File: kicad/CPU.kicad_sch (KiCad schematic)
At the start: 7 parts

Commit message: KiCad updates
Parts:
- removed U? (x6): 74LS245, symbol 74xx:74LS245
- added U? (x2): AS6C4008-55PCN, Package_DIP:DIP-32_W15.24mm, symbol Memory_RAM:AS6C4008-55PCN
- added U? (x2): SST39SF040, symbol Memory_Flash:SST39SF040
- added U?: GAL22V10, symbol Lattice_GAL_sym:GAL22V10
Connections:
- net A1: now also U?.12 (A0), U?.12 (A0), U?.12 (A0), U?.12 (A0)
- net A10: now also U?.26 (A9), U?.26 (A9), U?.26 (A9), U?.26 (A9)
- net A11: now also U?.23 (A10), U?.23 (A10), U?.23 (A10), U?.23 (A10)
- net A12: now also U?.25 (A11), U?.25 (A11), U?.25 (A11), U?.25 (A11)
- net A13: now also U?.4 (A12), U?.4 (A12), U?.4 (A12), U?.4 (A12)
- net A14: now also U?.28 (A13), U?.28 (A13), U?.28 (A13), U?.28 (A13)
- net A15: now also U?.29 (A14), U?.29 (A14), U?.3 (A14), U?.3 (A14)
- net A16: now also U?.3 (A15), U?.3 (A15), U?.31 (A15), U?.31 (A15)
- net A17: now also U?.2 (A16), U?.2 (A16), U?.2 (A16), U?.2 (A16)
- net A18: now also U?.30 (A17), U?.30 (A17), U?.30 (A17), U?.30 (A17)
- net A19: now also U?.1 (A18), U?.1 (A18), U?.1 (A18), U?.1 (A18)
- net A2: now also U?.11 (A1), U?.11 (A1), U?.11 (A1), U?.11 (A1)
- net A20: now also U?.2 (I1)
- net A21: now also U?.3 (I2)
- net A22: now also U?.4 (I3)
- net A23: now also U?.5 (I4)
- net A3: now also U?.10 (A2), U?.10 (A2), U?.10 (A2), U?.10 (A2)
- net A4: now also U?.9 (A3), U?.9 (A3), U?.9 (A3), U?.9 (A3)
- net A5: now also U?.8 (A4), U?.8 (A4), U?.8 (A4), U?.8 (A4)
- net A6: now also U?.7 (A5), U?.7 (A5), U?.7 (A5), U?.7 (A5)
- net A7: now also U?.6 (A6), U?.6 (A6), U?.6 (A6), U?.6 (A6)
- net A8: now also U?.5 (A7), U?.5 (A7), U?.5 (A7), U?.5 (A7)
- net A9: now also U?.27 (A8), U?.27 (A8), U?.27 (A8), U?.27 (A8)
- net D0: now also U?.13 (D0), U?.13 (DQ0)
- net D1: now also U?.14 (D1), U?.14 (DQ1)
- net D10: now also U?.15 (D2), U?.15 (DQ2)
- net D11: now also U?.17 (D3), U?.17 (DQ3)
- net D12: now also U?.18 (D4), U?.18 (DQ4)
- net D13: now also U?.19 (D5), U?.19 (DQ5)
- net D14: now also U?.20 (D6), U?.20 (DQ6)
- net D15: now also U?.21 (D7), U?.21 (DQ7)
- net D2: now also U?.15 (D2), U?.15 (DQ2)
- net D3: now also U?.17 (D3), U?.17 (DQ3)
- net D4: now also U?.18 (D4), U?.18 (DQ4)
- net D5: now also U?.19 (D5), U?.19 (DQ5)
- net D6: now also U?.20 (D6), U?.20 (DQ6)
- net D7: now also U?.21 (D7), U?.21 (DQ7)
- net D8: now also U?.13 (D0), U?.13 (DQ0)
- net D9: now also U?.14 (D1), U?.14 (DQ1)
- net GND: now also U?.12 (GND), U?.16 (GND), U?.16 (GND), U?.16 (VSS), U?.16 (VSS)
- net R/~{W}: now also U?.9 (R/W), U?.8 (I7)
- net VCC: now also U?.24 (VCC), U?.31 (PGM), U?.31 (PGM), U?.32 (VCC), U?.32 (VCC), U?.32 (VCC), U?.32 (VCC)
- net ~{AS}: now also U?.6 (AS), U?.6 (I5)
- net ~{LDS}: now also U?.8 (LDS), U?.7 (I6)
- net ~{UDS}: now also U?.7 (UDS), U?.9 (I8)
- new net ~{DUARTSEL}: U?.16 (I/O)
- new net ~{EVENREAD}: U?.18 (I/O), U?.24 (OE#), U?.24 (OE)
- new net ~{EVENWRITE}: U?.19 (I/O), U?.29 (WE#)
- new net ~{ODDREAD}: U?.17 (I/O), U?.24 (OE#), U?.24 (OE)
- new net ~{ODDWRITE}: U?.21 (I/O), U?.29 (WE#)
- new net ~{RAM0SEL}: U?.15 (I/O), U?.22 (CE#), U?.22 (CE#)
- new net ~{ROMSEL}: U?.14 (I/O), U?.22 (CE)
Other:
- note added: "EVEN"
- note added: "ODD"

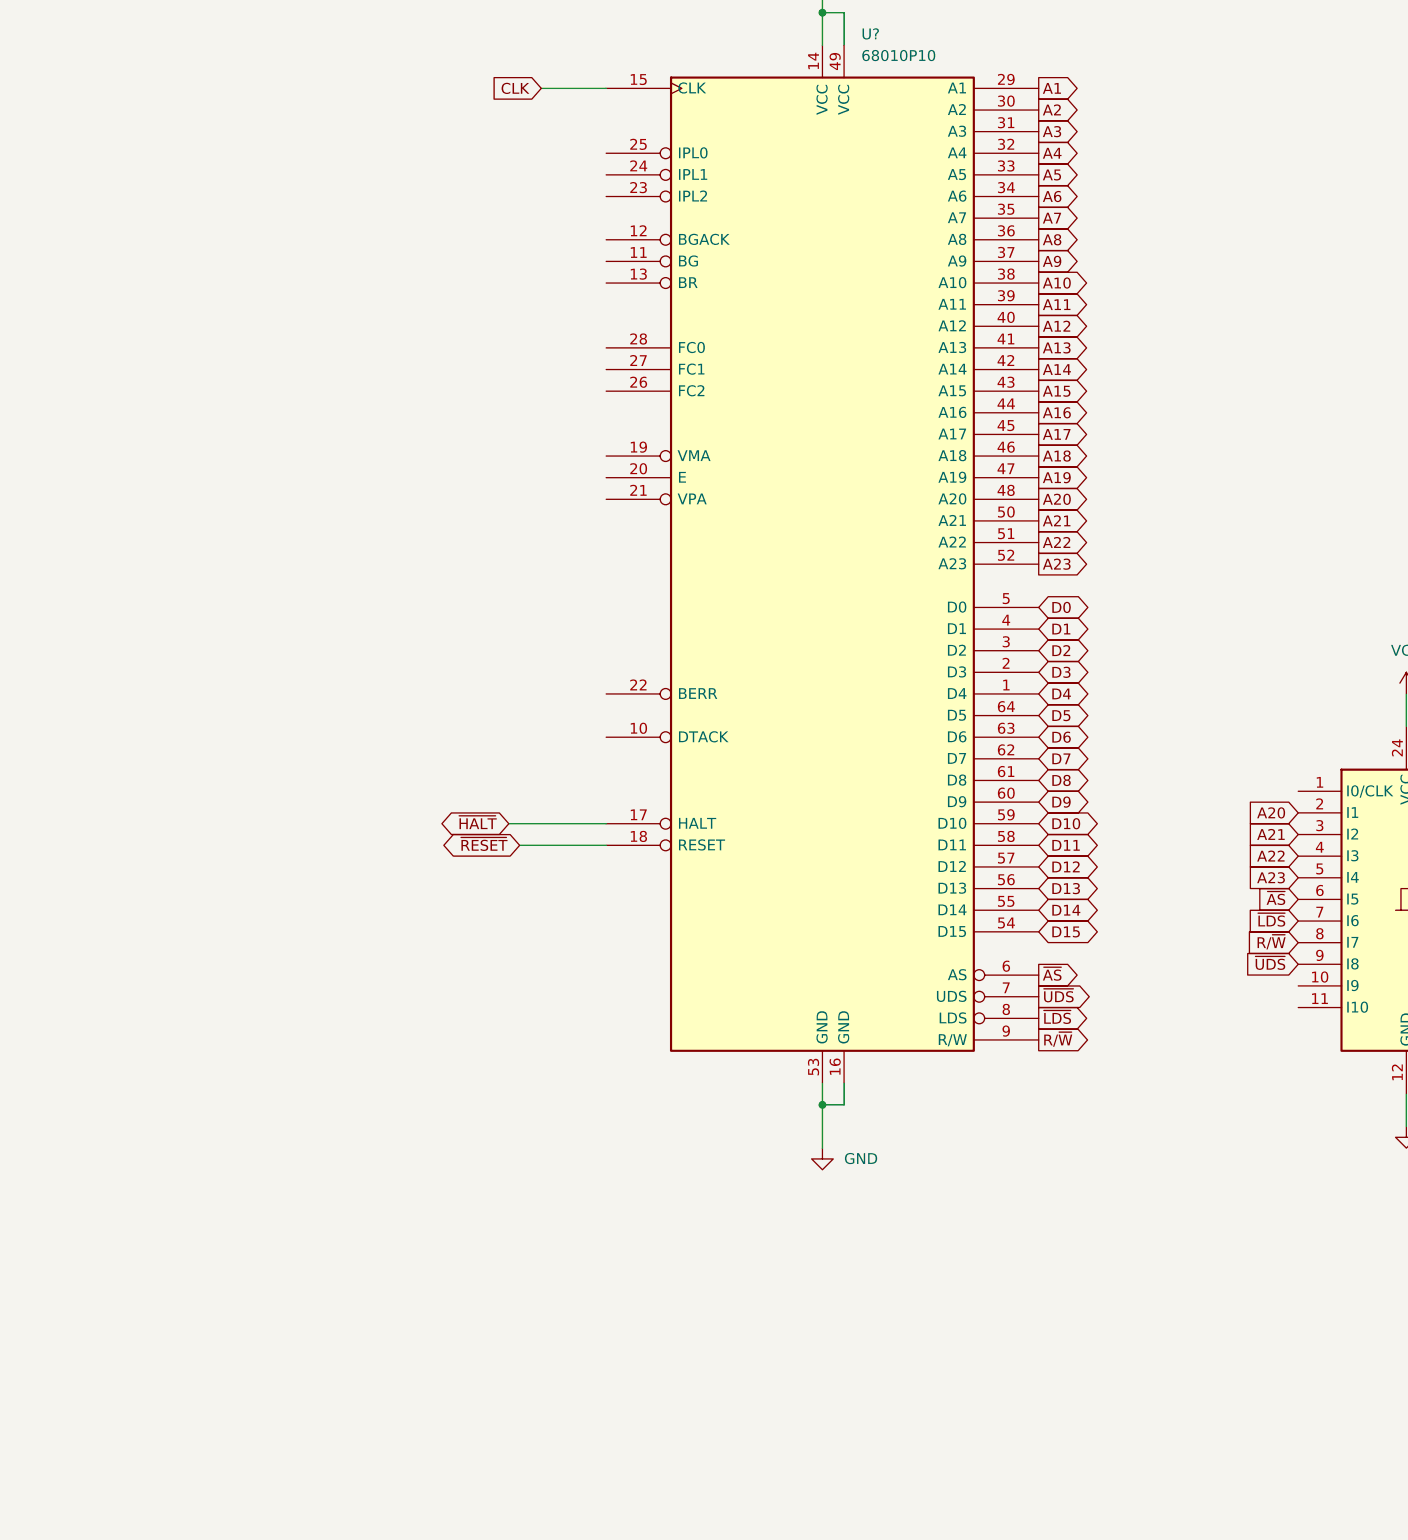
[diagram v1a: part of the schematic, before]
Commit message: Update kicad
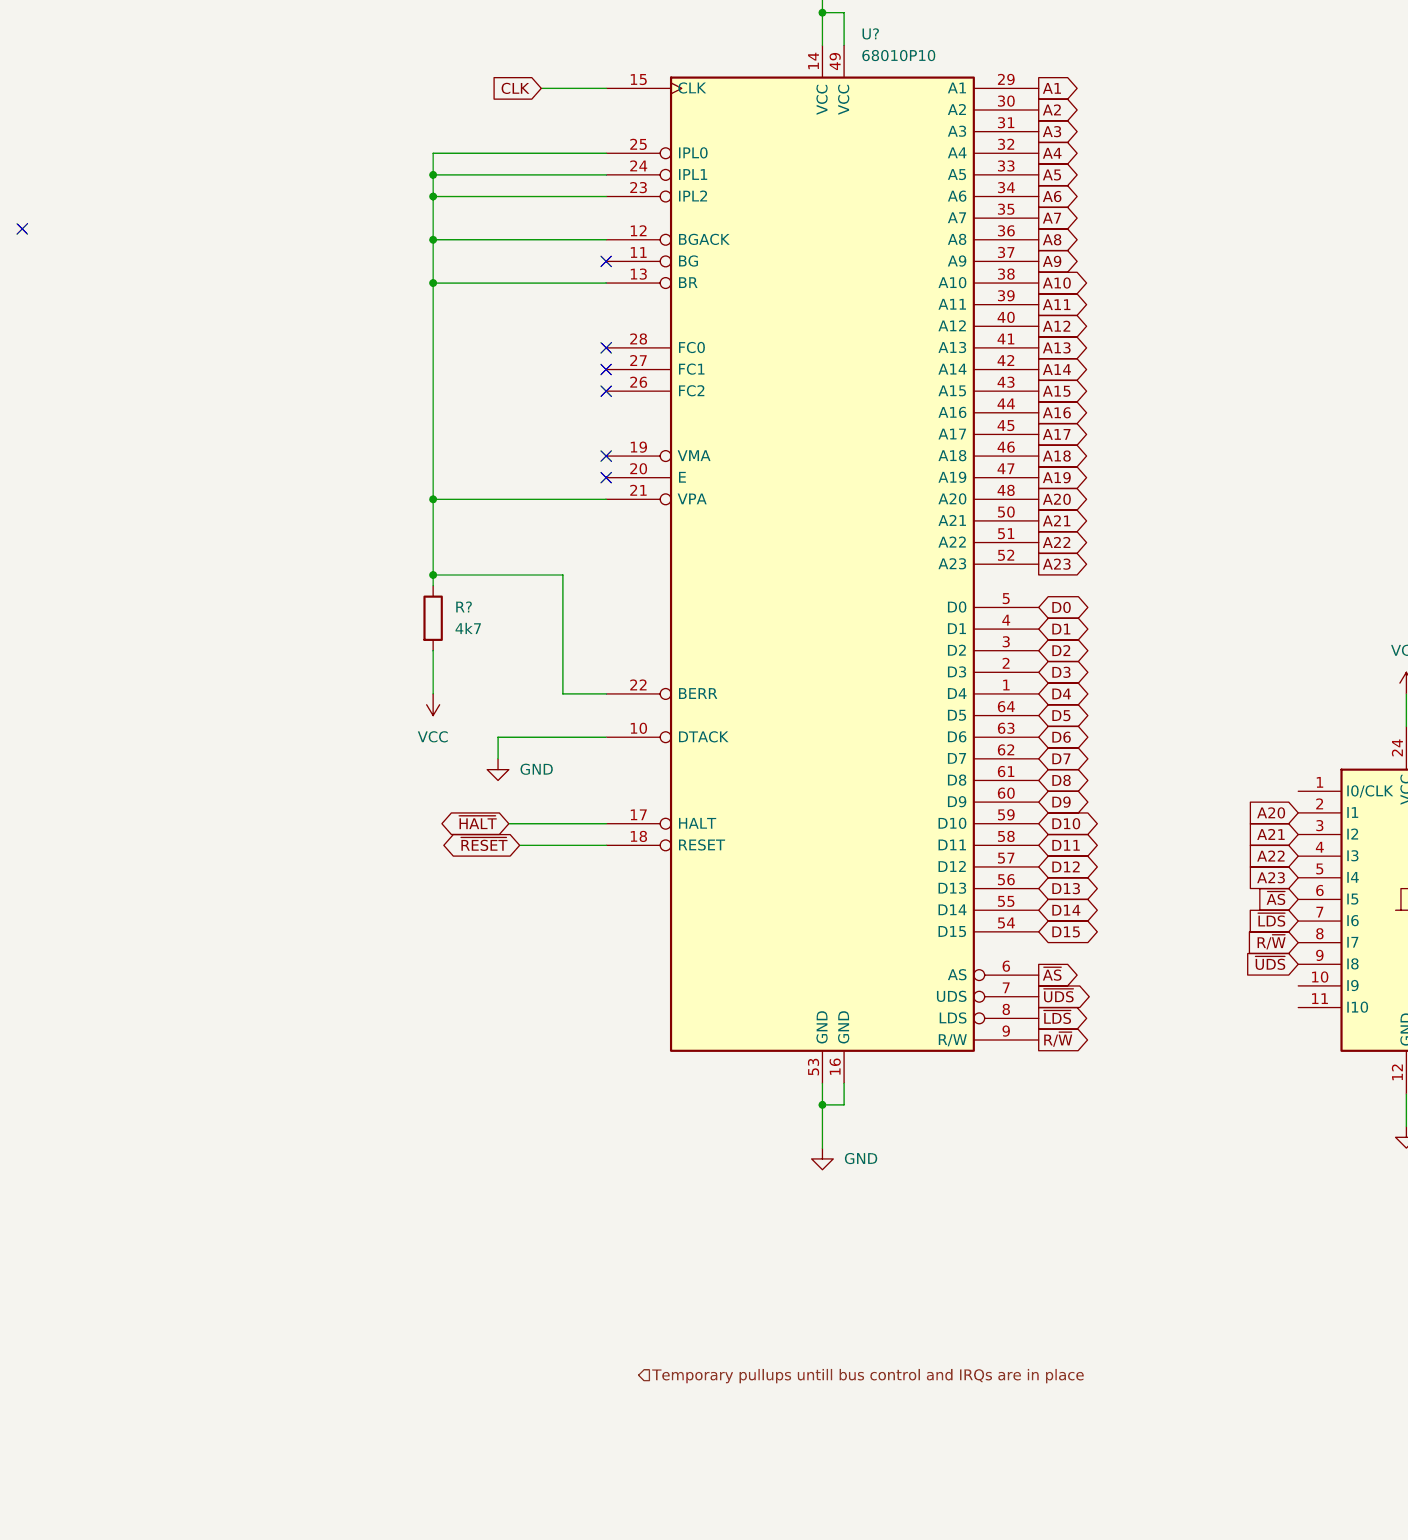
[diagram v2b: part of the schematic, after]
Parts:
- added R?: 4k7, symbol Device:R
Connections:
- net GND: now also U?.10 (DTACK)
- net VCC: now also R?.2
- net at U?.12 (BGACK): now also U?.13 (BR), U?.21 (VPA), U?.22 (BERR), U?.23 (IPL2), U?.24 (IPL1), U?.25 (IPL0), R?.1
- no-connect marks 0 -> 7
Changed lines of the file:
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@@
 (kicad_sch (version 20211123) (generator eeschema)
   (paper "A3")
+  (junction (at 20.32 80.01) (diameter 0) (color 0 0 0 0)
+  )
+  (junction (at 20.32 44.45) (diameter 0) (color 0 0 0 0)
+  )
+  (junction (at 20.32 41.91) (diameter 0) (color 0 0 0 0)
+  )
+  (junction (at 20.32 49.53) (diameter 0) (color 0 0 0 0)
+  )
   (junction (at 316.23 36.83) (diameter 0) (color 0 0 0 0)
   )
@@
   (junction (at 66.04 22.86) (diameter 0) (color 0 0 0 0)
   )
+  (junction (at 20.32 88.9) (diameter 0) (color 0 0 0 0)
+  )
+  (junction (at 20.32 54.61) (diameter 0) (color 0 0 0 0)
+  )
+  (no_connect (at 40.64 77.47))
+  (no_connect (at 40.64 62.23))
+  (no_connect (at 40.64 64.77))
+  (no_connect (at 40.64 74.93))
+  (no_connect (at -27.94 48.26))
+  (no_connect (at 40.64 52.07))
+  (no_connect (at 40.64 67.31))
   (wire (pts (xy 316.23 34.29) (xy 316.23 36.83))
     (stroke (width 0) (type default) (color 0 0 0 0))
   )
+  (wire (pts (xy 40.64 41.91) (xy 20.32 41.91))
+    (stroke (width 0) (type default) (color 0 0 0 0))
+  )
   (wire (pts (xy 66.04 22.86) (xy 68.58 22.86))
     (stroke (width 0) (type default) (color 0 0 0 0))
@@
     (stroke (width 0) (type default) (color 0 0 0 0))
   )
+  (wire (pts (xy 20.32 49.53) (xy 20.32 54.61))
+    (stroke (width 0) (type default) (color 0 0 0 0))
+  )
   (wire (pts (xy 66.04 22.86) (xy 66.04 26.67))
     (stroke (width 0) (type default) (color 0 0 0 0))
   )
+  (wire (pts (xy 20.32 54.61) (xy 20.32 80.01))
+    (stroke (width 0) (type default) (color 0 0 0 0))
+  )
   (wire (pts (xy 316.23 36.83) (xy 316.23 48.26))
     (stroke (width 0) (type default) (color 0 0 0 0))
@@
     (stroke (width 0) (type default) (color 0 0 0 0))
   )
+  (wire (pts (xy 35.56 102.87) (xy 35.56 88.9))
+    (stroke (width 0) (type default) (color 0 0 0 0))
+  )
+  (wire (pts (xy 20.32 54.61) (xy 40.64 54.61))
+    (stroke (width 0) (type default) (color 0 0 0 0))
+  )
+  (wire (pts (xy 40.64 107.95) (xy 27.94 107.95))
+    (stroke (width 0) (type default) (color 0 0 0 0))
+  )
   (wire (pts (xy 262.89 147.32) (xy 262.89 154.94))
     (stroke (width 0) (type default) (color 0 0 0 0))
@@
     (stroke (width 0) (type default) (color 0 0 0 0))
   )
+  (wire (pts (xy 40.64 44.45) (xy 20.32 44.45))
+    (stroke (width 0) (type default) (color 0 0 0 0))
+  )
+  (wire (pts (xy 20.32 49.53) (xy 40.64 49.53))
+    (stroke (width 0) (type default) (color 0 0 0 0))
+  )
+  (wire (pts (xy 20.32 97.79) (xy 20.32 102.87))
+    (stroke (width 0) (type default) (color 0 0 0 0))
+  )
+  (wire (pts (xy 20.32 44.45) (xy 20.32 49.53))
+    (stroke (width 0) (type default) (color 0 0 0 0))
+  )
+  (wire (pts (xy 20.32 39.37) (xy 20.32 41.91))
+    (stroke (width 0) (type default) (color 0 0 0 0))
+  )
   (wire (pts (xy 240.03 36.83) (xy 265.43 36.83))
     (stroke (width 0) (type default) (color 0 0 0 0))
   )
+  (wire (pts (xy 20.32 41.91) (xy 20.32 44.45))
+    (stroke (width 0) (type default) (color 0 0 0 0))
+  )
   (wire (pts (xy 316.23 111.76) (xy 316.23 118.11))
     (stroke (width 0) (type default) (color 0 0 0 0))
@@
     (stroke (width 0) (type default) (color 0 0 0 0))
   )
+  (wire (pts (xy 20.32 80.01) (xy 20.32 88.9))
+    (stroke (width 0) (type default) (color 0 0 0 0))
+  )
   (wire (pts (xy 66.04 20.32) (xy 66.04 22.86))
     (stroke (width 0) (type default) (color 0 0 0 0))
   )
+  (wire (pts (xy 27.94 107.95) (xy 27.94 110.49))
+    (stroke (width 0) (type default) (color 0 0 0 0))
+  )
+  (wire (pts (xy 35.56 88.9) (xy 20.32 88.9))
+    (stroke (width 0) (type default) (color 0 0 0 0))
+  )
   (wire (pts (xy 134.62 149.86) (xy 134.62 153.67))
     (stroke (width 0) (type default) (color 0 0 0 0))
@@
     (stroke (width 0) (type default) (color 0 0 0 0))
   )
+  (wire (pts (xy 40.64 102.87) (xy 35.56 102.87))
+    (stroke (width 0) (type default) (color 0 0 0 0))
+  )
   (wire (pts (xy 300.99 101.6) (xy 290.83 101.6))
     (stroke (width 0) (type default) (color 0 0 0 0))
@@
   )
   (wire (pts (xy 314.96 210.82) (xy 314.96 218.44))
+    (stroke (width 0) (type default) (color 0 0 0 0))
+  )
+  (wire (pts (xy 20.32 88.9) (xy 20.32 90.17))
+    (stroke (width 0) (type default) (color 0 0 0 0))
+  )
+  (wire (pts (xy 40.64 39.37) (xy 20.32 39.37))
+    (stroke (width 0) (type default) (color 0 0 0 0))
+  )
+  (wire (pts (xy 20.32 80.01) (xy 40.64 80.01))
     (stroke (width 0) (type default) (color 0 0 0 0))
   )
@@
       (effects (font (size 1.27 1.27)) (justify left) hide)
     )
+  )
+  (hierarchical_label "Temporary pullups untill bus control and IRQs are in place" (shape input)
+    (at 44.45 182.88 0)
+    (effects (font (size 1.27 1.27)) (justify left))
   )
   (symbol (lib_id "power:VCC") (at 265.43 34.29 0) (unit 1)
@@
     (pin "8")
     (pin "9")
+  )
+  (symbol (lib_id "power:GND") (at 27.94 110.49 0) (unit 1)
+    (in_bom yes) (on_board yes) (fields_autoplaced)
+    (property "Reference" "#PWR?" (id 0) (at 27.94 116.84 0)
+      (effects (font (size 1.27 1.27)) hide)
+    )
+    (property "Value" "GND" (id 1) (at 30.48 111.7599 0)
+      (effects (font (size 1.27 1.27)) (justify left))
+    )
+    (property "Footprint" "" (id 2) (at 27.94 110.49 0)
+      (effects (font (size 1.27 1.27)) hide)
+    )
+    (property "Datasheet" "" (id 3) (at 27.94 110.49 0)
+      (effects (font (size 1.27 1.27)) hide)
+    )
+    (pin "1")
   )
   (symbol (lib_id "Memory_Flash:SST39SF040") (at 265.43 81.28 0) (unit 1)
@@
     (pin "9")
   )
+  (symbol (lib_id "power:VCC") (at 20.32 102.87 180) (unit 1)
+    (in_bom yes) (on_board yes) (fields_autoplaced)
+    (property "Reference" "#PWR?" (id 0) (at 20.32 99.06 0)
+      (effects (font (size 1.27 1.27)) hide)
+    )
+    (property "Value" "VCC" (id 1) (at 20.32 107.95 0))
+    (property "Footprint" "" (id 2) (at 20.32 102.87 0)
+      (effects (font (size 1.27 1.27)) hide)
+    )
+    (property "Datasheet" "" (id 3) (at 20.32 102.87 0)
+      (effects (font (size 1.27 1.27)) hide)
+    )
+    (pin "1")
+  )
   (symbol (lib_id "Lattice_GAL_sym:GAL22V10") (at 134.62 127 0) (unit 1)
     (in_bom yes) (on_board yes) (fields_autoplaced)
@@
     (pin "1")
   )
+  (symbol (lib_id "Device:R") (at 20.32 93.98 0) (unit 1)
+    (in_bom yes) (on_board yes) (fields_autoplaced)
+    (property "Reference" "R?" (id 0) (at 22.86 92.7099 0)
+      (effects (font (size 1.27 1.27)) (justify left))
+    )
+    (property "Value" "4k7" (id 1) (at 22.86 95.2499 0)
+      (effects (font (size 1.27 1.27)) (justify left))
+    )
+    (property "Footprint" "" (id 2) (at 18.542 93.98 90)
+      (effects (font (size 1.27 1.27)) hide)
+    )
+    (property "Datasheet" "~" (id 3) (at 20.32 93.98 0)
+      (effects (font (size 1.27 1.27)) hide)
+    )
+    (pin "1")
+    (pin "2")
+  )
   (symbol (lib_id "power:VCC") (at 262.89 147.32 0) (unit 1)

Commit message: started with pcb
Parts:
- added C10, C11, C6, C7, C8, C9: 100nF, Capacitor_THT:CP_Radial_D8.0mm_P5.00mm, symbol Device:C
- R8: renamed from R?; footprint (none) -> Resistor_THT:R_Axial_DIN0207_L6.3mm_D2.5mm_P10.16mm_Horizontal
- U3: renamed from U?; footprint (none) -> matsb:MC68000-DIL64
- U4: renamed from U?; footprint (none) -> Package_DIP:DIP-24_W7.62mm_Socket
- U5, U7: renamed from U?; footprint (none) -> Package_DIP:DIP-32_W15.24mm_Socket
- U6, U8: renamed from U?; footprint Package_DIP:DIP-32_W15.24mm -> Package_DIP:DIP-32_W15.24mm_Socket
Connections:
- net GND: now also C10.2, C11.2, C6.2, C7.2, C8.2, C9.2
- net VCC: now also R8.1, C10.1, C11.1, C6.1, C7.1, C8.1, C9.1; no longer R8.2
- net ~{ROMSEL}: now also U7.22 (CE)
- net at U3.12 (BGACK), U3.13 (BR), U3.21 (VPA)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: now also R8.2; no longer R8.1
- no-connect marks 7 -> 14
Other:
- note added: "Temporary pullups untill bus control and IRQs are in place"
- title: (none) -> Mats Brorson 68010 SBC CPU
- moved on the sheet: R8, U5, U7

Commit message: Update footprint
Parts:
- C10, C11, C6, C7, C8, C9: footprint Capacitor_THT:CP_Radial_D8.0mm_P5.00mm -> Capacitor_THT:CP_Radial_D5.0mm_P2.50mm
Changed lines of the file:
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@@
       (effects (font (size 1.27 1.27)) (justify left))
     )
-    (property "Footprint" "Capacitor_THT:CP_Radial_D8.0mm_P5.00mm" (id 2) (at 160.9852 67.31 0)
+    (property "Footprint" "Capacitor_THT:CP_Radial_D5.0mm_P2.50mm" (id 2) (at 160.9852 67.31 0)
       (effects (font (size 1.27 1.27)) hide)
     )
@@
       (effects (font (size 1.27 1.27)) (justify left))
     )
-    (property "Footprint" "Capacitor_THT:CP_Radial_D8.0mm_P5.00mm" (id 2) (at 148.2852 67.31 0)
+    (property "Footprint" "Capacitor_THT:CP_Radial_D5.0mm_P2.50mm" (id 2) (at 148.2852 67.31 0)
       (effects (font (size 1.27 1.27)) hide)
     )
@@
       (effects (font (size 1.27 1.27)) (justify left))
     )
-    (property "Footprint" "Capacitor_THT:CP_Radial_D8.0mm_P5.00mm" (id 2) (at 173.6852 67.31 0)
+    (property "Footprint" "Capacitor_THT:CP_Radial_D5.0mm_P2.50mm" (id 2) (at 173.6852 67.31 0)
       (effects (font (size 1.27 1.27)) hide)
     )
@@
       (effects (font (size 1.27 1.27)) (justify left))
     )
-    (property "Footprint" "Capacitor_THT:CP_Radial_D8.0mm_P5.00mm" (id 2) (at 186.3852 67.31 0)
+    (property "Footprint" "Capacitor_THT:CP_Radial_D5.0mm_P2.50mm" (id 2) (at 186.3852 67.31 0)
       (effects (font (size 1.27 1.27)) hide)
     )
@@
       (effects (font (size 1.27 1.27)) (justify left))
     )
-    (property "Footprint" "Capacitor_THT:CP_Radial_D8.0mm_P5.00mm" (id 2) (at 135.5852 67.31 0)
+    (property "Footprint" "Capacitor_THT:CP_Radial_D5.0mm_P2.50mm" (id 2) (at 135.5852 67.31 0)
       (effects (font (size 1.27 1.27)) hide)
     )
@@
       (effects (font (size 1.27 1.27)) (justify left))
     )
-    (property "Footprint" "Capacitor_THT:CP_Radial_D8.0mm_P5.00mm" (id 2) (at 199.0852 67.31 0)
-      (effects (font (size 1.27 1.27)) hide)
-    )
+    (property "Footprint" "Capacitor_THT:CP_Radial_D5.0mm_P2.50mm" (id 2) (at 199.0852 67.31 0)
+      (effects (font (size 1.27 1.27)) hide)
+    )

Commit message: cleanup
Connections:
- net GND: no longer U3.10 (DTACK)
- net FC2: now reaches U3.26 (FC2)
- net FC1: now reaches U3.27 (FC1)
- net FC0: now reaches U3.28 (FC0)
- new net ~{DTACK}: U3.10 (DTACK)
- no-connect marks 14 -> 11
